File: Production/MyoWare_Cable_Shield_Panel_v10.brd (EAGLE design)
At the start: 210.8 x 85.3 mm, 273 parts

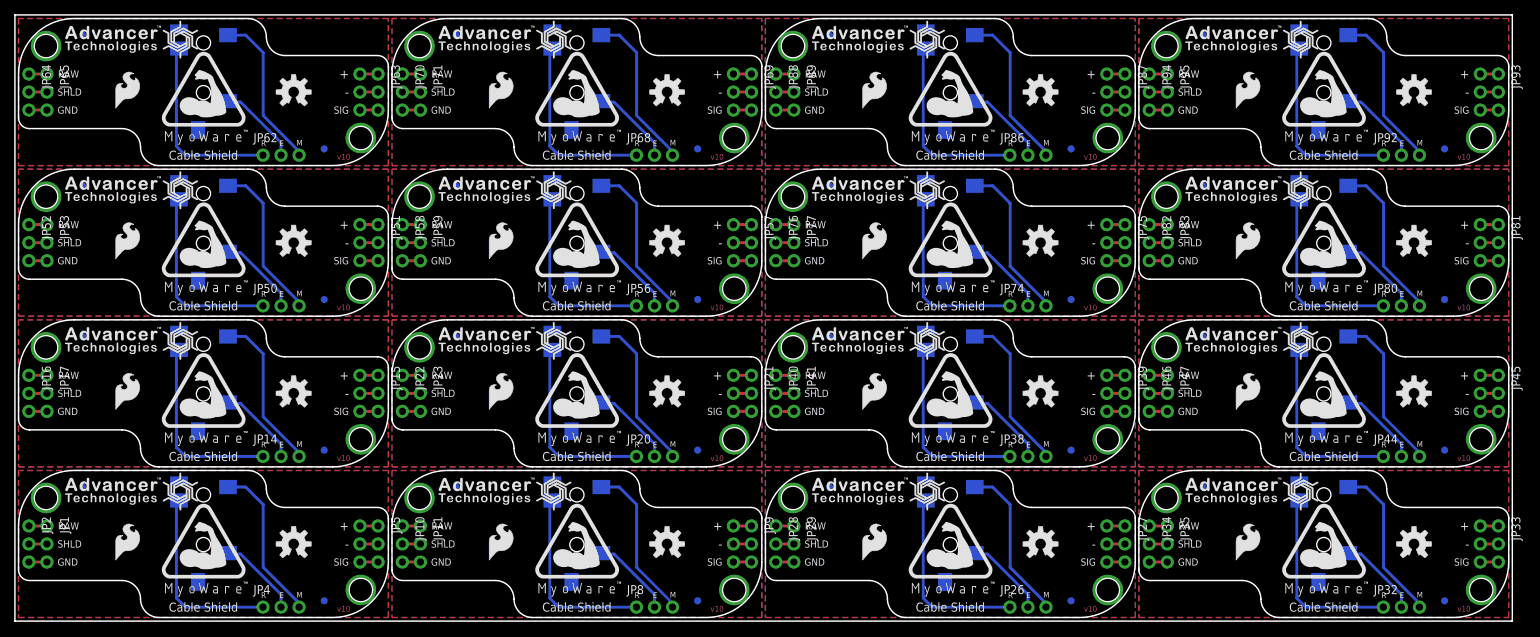
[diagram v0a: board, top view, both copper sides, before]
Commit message: removing old panel and test panel
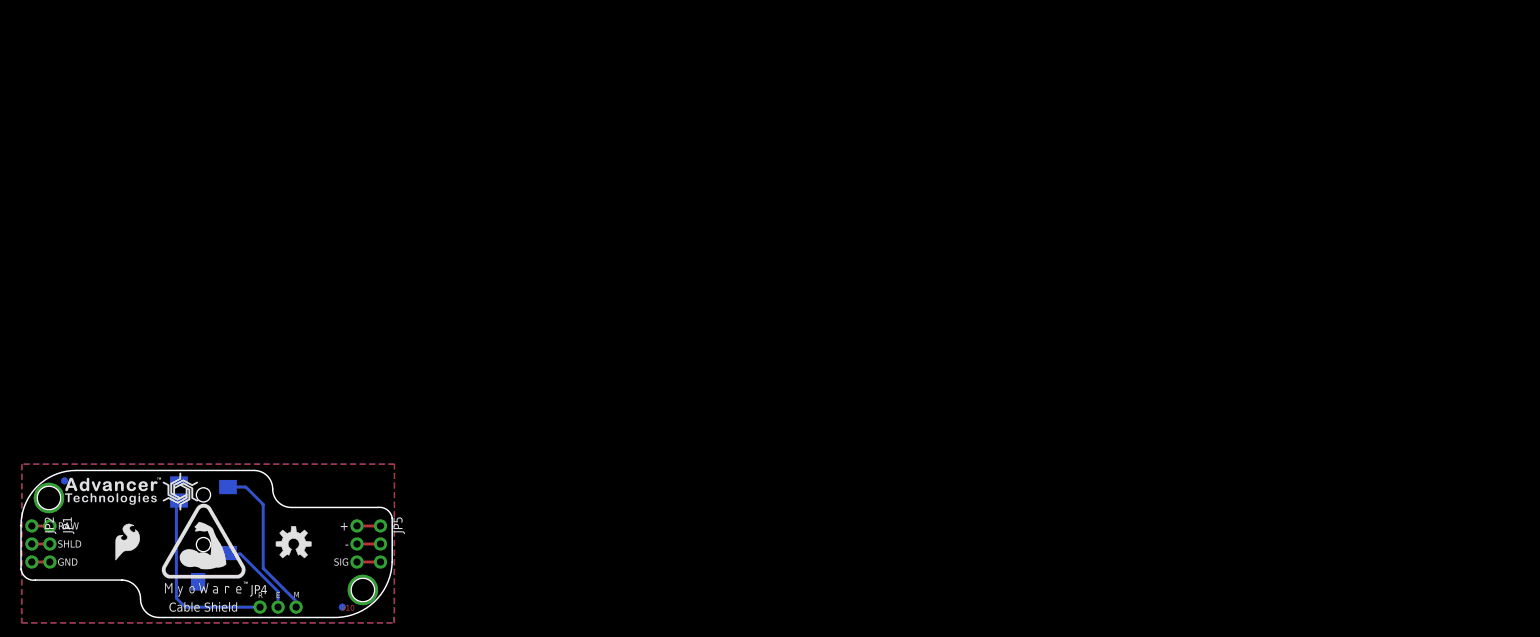
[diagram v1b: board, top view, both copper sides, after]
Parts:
- removed FID10, FID11, FID12, FID13, FID14, FID15, FID16, FID17, FID18, FID19, FID20, FID21, FID22, FID23, FID24, FID25, FID26, FID27, FID28, FID29, FID3, FID30, FID31, FID32, FID4, FID5, FID6, FID7, FID8, FID9: FIDUCIAL1X2, SparkFun-Aesthetics:FIDUCIAL-1X2
- removed JP10, JP11, JP13, JP14, JP15, JP16, JP17, JP19, JP20, JP21, JP22, JP23, JP25, JP26, JP27, JP28, JP29, JP31, JP32, JP33, JP34, JP35, JP37, JP38, JP39, JP40, JP41, JP43, JP44, JP45, JP46, JP47, JP49, JP50, JP51, JP52, JP53, JP55, JP56, JP57, JP58, JP59, JP61, JP62, JP63, JP64, JP65, JP67, JP68, JP69, JP7, JP70, JP71, JP73, JP74, JP75, JP76, JP77, JP79, JP8, JP80, JP81, JP82, JP83, JP85, JP86, JP87, JP88, JP89, JP9, JP91, JP92, JP93, JP94, JP95: Power, SparkFun-Connectors:1X03_NO_SILK
- removed JP12, JP18, JP24, JP30, JP36, JP42, JP48, JP54, JP60, JP66, JP72, JP78, JP84, JP90, JP96: 3.5mm Jack, SparkFun-Connectors:AUDIO-JACK-3.5MM-SMD
- removed LOGO10, LOGO13, LOGO16, LOGO19, LOGO22, LOGO25, LOGO28, LOGO31, LOGO34, LOGO37, LOGO4, LOGO40, LOGO43, LOGO46, LOGO7: OSHW-LOGOM, SparkFun-Aesthetics:OSHW-LOGO-M
- removed LOGO11, LOGO14, LOGO17, LOGO20, LOGO23, LOGO26, LOGO29, LOGO32, LOGO35, LOGO38, LOGO41, LOGO44, LOGO47, LOGO5, LOGO8: SFE_LOGO_FLAME.2_INCH, SparkFun-Aesthetics:SFE_LOGO_FLAME_.2
- removed LOGO12, LOGO15, LOGO18, LOGO21, LOGO24, LOGO27, LOGO3, LOGO30, LOGO33, LOGO36, LOGO39, LOGO42, LOGO45, LOGO6, LOGO9: (no value), advancer-technologies:MYOWARE_LOGO
- removed SPIRAL1, SPIRAL10, SPIRAL11, SPIRAL12, SPIRAL13, SPIRAL14, SPIRAL15, SPIRAL2, SPIRAL3, SPIRAL4, SPIRAL5, SPIRAL6, SPIRAL7, SPIRAL8, SPIRAL9: (no value), advancer-technologies:SPIRAL_LOGO_60%
- removed STANDOFF10, STANDOFF11, STANDOFF12, STANDOFF13, STANDOFF14, STANDOFF15, STANDOFF16, STANDOFF17, STANDOFF18, STANDOFF19, STANDOFF20, STANDOFF21, STANDOFF22, STANDOFF23, STANDOFF24, STANDOFF25, STANDOFF26, STANDOFF27, STANDOFF28, STANDOFF29, STANDOFF3, STANDOFF30, STANDOFF31, STANDOFF32, STANDOFF4, STANDOFF5, STANDOFF6, STANDOFF7, STANDOFF8, STANDOFF9: STAND-OFF, SparkFun-Electromechanical:STAND-OFF
- removed U$1, U$10, U$13, U$16, U$19, U$22, U$25, U$28, U$31, U$34, U$37, U$40, U$43, U$46, U$7: (no value), SparkFun-Aesthetics:NO_PB_LOGO_0.120
- removed U$11, U$14, U$17, U$2, U$20, U$23, U$26, U$29, U$32, U$35, U$38, U$41, U$44, U$47, U$8: (no value), advancer-technologies:ADVANCER_LOGO
- removed U$12, U$15, U$18, U$21, U$24, U$27, U$30, U$33, U$36, U$39, U$4, U$42, U$45, U$48, U$9: (no value), SparkFun-Aesthetics:ROHS_LOGO_0.18_IN
- moved FID1 2.71 mm to (19.6, -8.89)
- moved FID2 2.71 mm to (-19.6, 8.89)
- moved JP1 0.41 mm to (-21.6, 2.54)
- moved JP6 0.41 mm to (21.6, 2.54)
- moved JP4 0.41 mm to (7.97, -8.89)
- moved JP2 0.41 mm to (-24.2, 2.54)
- moved STANDOFF1 0.41 mm to (-21.7, 6.48)
- moved JP5 0.35 mm to (24.9, 2.54)
- moved STANDOFF2 0.29 mm to (22.4, -6.48)
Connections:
- removed net END1: JP12.TIP, JP8.2
- removed net END10: JP62.2, JP66.TIP
- removed net END11: JP68.2, JP72.TIP
- removed net END12: JP74.2, JP78.TIP
- removed net END13: JP80.2, JP84.TIP
- removed net END14: JP86.2, JP90.TIP
- removed net END15: JP92.2, JP96.TIP
- removed net END2: JP14.2, JP18.TIP
- removed net END3: JP20.2, JP24.TIP
- removed net END4: JP26.2, JP30.TIP
- removed net END5: JP32.2, JP36.TIP
- removed net END6: JP38.2, JP42.TIP
- removed net END7: JP44.2, JP48.TIP
- removed net END8: JP50.2, JP54.TIP
- removed net END9: JP56.2, JP60.TIP
- removed net GND1: JP10.3, JP11.3, JP7.2, JP9.2
- removed net GND10: JP61.2, JP63.2, JP64.3, JP65.3
- removed net GND11: JP67.2, JP69.2, JP70.3, JP71.3
- removed net GND12: JP73.2, JP75.2, JP76.3, JP77.3
- removed net GND13: JP79.2, JP81.2, JP82.3, JP83.3
- removed net GND14: JP85.2, JP87.2, JP88.3, JP89.3
- removed net GND15: JP91.2, JP93.2, JP94.3, JP95.3
- removed net GND2: JP13.2, JP15.2, JP16.3, JP17.3
- removed net GND3: JP19.2, JP21.2, JP22.3, JP23.3
- removed net GND4: JP25.2, JP27.2, JP28.3, JP29.3
- removed net GND5: JP31.2, JP33.2, JP34.3, JP35.3
- removed net GND6: JP37.2, JP39.2, JP40.3, JP41.3
- removed net GND7: JP43.2, JP45.2, JP46.3, JP47.3
- removed net GND8: JP49.2, JP51.2, JP52.3, JP53.3
- removed net GND9: JP55.2, JP57.2, JP58.3, JP59.3
- removed net MID1: JP12.SLEEVE, JP8.3
- removed net MID10: JP62.3, JP66.SLEEVE
- removed net MID11: JP68.3, JP72.SLEEVE
- removed net MID12: JP74.3, JP78.SLEEVE
- removed net MID13: JP80.3, JP84.SLEEVE
- removed net MID14: JP86.3, JP90.SLEEVE
- removed net MID15: JP92.3, JP96.SLEEVE
- removed net MID2: JP14.3, JP18.SLEEVE
- removed net MID3: JP20.3, JP24.SLEEVE
- removed net MID4: JP26.3, JP30.SLEEVE
- removed net MID5: JP32.3, JP36.SLEEVE
- removed net MID6: JP38.3, JP42.SLEEVE
- removed net MID7: JP44.3, JP48.SLEEVE
- removed net MID8: JP50.3, JP54.SLEEVE
- removed net MID9: JP56.3, JP60.SLEEVE
- removed net RAW1: JP10.1, JP11.1
- removed net RAW10: JP64.1, JP65.1
- removed net RAW11: JP70.1, JP71.1
- removed net RAW12: JP76.1, JP77.1
- removed net RAW13: JP82.1, JP83.1
- removed net RAW14: JP88.1, JP89.1
- removed net RAW15: JP94.1, JP95.1
- removed net RAW2: JP16.1, JP17.1
- removed net RAW3: JP22.1, JP23.1
- removed net RAW4: JP28.1, JP29.1
- removed net RAW5: JP34.1, JP35.1
- removed net RAW6: JP40.1, JP41.1
- removed net RAW7: JP46.1, JP47.1
- removed net RAW8: JP52.1, JP53.1
- removed net RAW9: JP58.1, JP59.1
- removed net SHIELD1: JP10.2, JP11.2
- removed net SHIELD10: JP64.2, JP65.2
- removed net SHIELD11: JP70.2, JP71.2
- removed net SHIELD12: JP76.2, JP77.2
- removed net SHIELD13: JP82.2, JP83.2
- removed net SHIELD14: JP88.2, JP89.2
- removed net SHIELD15: JP94.2, JP95.2
- removed net SHIELD2: JP16.2, JP17.2
- removed net SHIELD3: JP22.2, JP23.2
- removed net SHIELD4: JP28.2, JP29.2
- removed net SHIELD5: JP34.2, JP35.2
- removed net SHIELD6: JP40.2, JP41.2
- removed net SHIELD7: JP46.2, JP47.2
- removed net SHIELD8: JP52.2, JP53.2
- removed net SHIELD9: JP58.2, JP59.2
- removed net SIG1: JP7.3, JP9.3
- removed net SIG10: JP61.3, JP63.3
- removed net SIG11: JP67.3, JP69.3
- removed net SIG12: JP73.3, JP75.3
- removed net SIG13: JP79.3, JP81.3
- removed net SIG14: JP85.3, JP87.3
- removed net SIG15: JP91.3, JP93.3
- removed net SIG2: JP13.3, JP15.3
- removed net SIG3: JP19.3, JP21.3
- removed net SIG4: JP25.3, JP27.3
- removed net SIG5: JP31.3, JP33.3
- removed net SIG6: JP37.3, JP39.3
- removed net SIG7: JP43.3, JP45.3
- removed net SIG8: JP49.3, JP51.3
- removed net SIG9: JP55.3, JP57.3
- removed net VCC1: JP7.1, JP9.1
- removed net VCC10: JP61.1, JP63.1
- removed net VCC11: JP67.1, JP69.1
- removed net VCC12: JP73.1, JP75.1
- removed net VCC13: JP79.1, JP81.1
- removed net VCC14: JP85.1, JP87.1
- removed net VCC15: JP91.1, JP93.1
- removed net VCC2: JP13.1, JP15.1
- removed net VCC3: JP19.1, JP21.1
- removed net VCC4: JP25.1, JP27.1
- removed net VCC5: JP31.1, JP33.1
- removed net VCC6: JP37.1, JP39.1
- removed net VCC7: JP43.1, JP45.1
- removed net VCC8: JP49.1, JP51.1
- removed net VCC9: JP55.1, JP57.1
- removed net VREF1: JP12.RING, JP8.1
- removed net VREF10: JP62.1, JP66.RING
- removed net VREF11: JP68.1, JP72.RING
- removed net VREF12: JP74.1, JP78.RING
- removed net VREF13: JP80.1, JP84.RING
- removed net VREF14: JP86.1, JP90.RING
- removed net VREF15: JP92.1, JP96.RING
- removed net VREF2: JP14.1, JP18.RING
- removed net VREF3: JP20.1, JP24.RING
- removed net VREF4: JP26.1, JP30.RING
- removed net VREF5: JP32.1, JP36.RING
- removed net VREF6: JP38.1, JP42.RING
- removed net VREF7: JP44.1, JP48.RING
- removed net VREF8: JP50.1, JP54.RING
- removed net VREF9: JP56.1, JP60.RING
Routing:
- net VREF7: track 26.7 -> 0.00 mm
- net VREF5: track 26.7 -> 0.00 mm
- net VREF3: track 26.7 -> 0.00 mm
- net VREF15: track 26.7 -> 0.00 mm
- net VREF11: track 26.7 -> 0.00 mm
- net VREF10: track 26.7 -> 0.00 mm
- net VREF9: track 26.7 -> 0.00 mm
- net VREF8: track 26.7 -> 0.00 mm
- net VREF2: track 26.7 -> 0.00 mm
- net VREF13: track 26.7 -> 0.00 mm
- net VREF1: track 26.7 -> 0.00 mm
- net VREF6: track 26.7 -> 0.00 mm
- net VREF14: track 26.7 -> 0.00 mm
- net VREF4: track 26.7 -> 0.00 mm
- net VREF12: track 26.7 -> 0.00 mm
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- removed copper zone on layer 1, net GND1
- removed copper zone on layer 16, net GND1
- removed copper zone on layer 1, net GND10
- removed copper zone on layer 16, net GND10
- removed copper zone on layer 1, net GND11
- removed copper zone on layer 16, net GND11
- removed copper zone on layer 1, net GND12
- removed copper zone on layer 16, net GND12
- removed copper zone on layer 1, net GND13
- removed copper zone on layer 16, net GND13
- removed copper zone on layer 1, net GND14
- removed copper zone on layer 16, net GND14
- removed copper zone on layer 1, net GND15
- removed copper zone on layer 16, net GND15
- removed copper zone on layer 1, net GND2
- removed copper zone on layer 16, net GND2
- removed copper zone on layer 1, net GND3
- removed copper zone on layer 16, net GND3
- removed copper zone on layer 1, net GND4
- removed copper zone on layer 16, net GND4
- removed copper zone on layer 1, net GND5
- removed copper zone on layer 16, net GND5
- removed copper zone on layer 1, net GND6
- removed copper zone on layer 16, net GND6
- removed copper zone on layer 1, net GND7
- removed copper zone on layer 16, net GND7
- removed copper zone on layer 1, net GND8
- removed copper zone on layer 16, net GND8
- removed copper zone on layer 1, net GND9
- removed copper zone on layer 16, net GND9
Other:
- board size 210.8 x 85.3 mm -> 52.3 x 20.7 mm
